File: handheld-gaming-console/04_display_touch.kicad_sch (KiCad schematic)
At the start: 3 parts, among them J7 DSI_15PIN_FPC

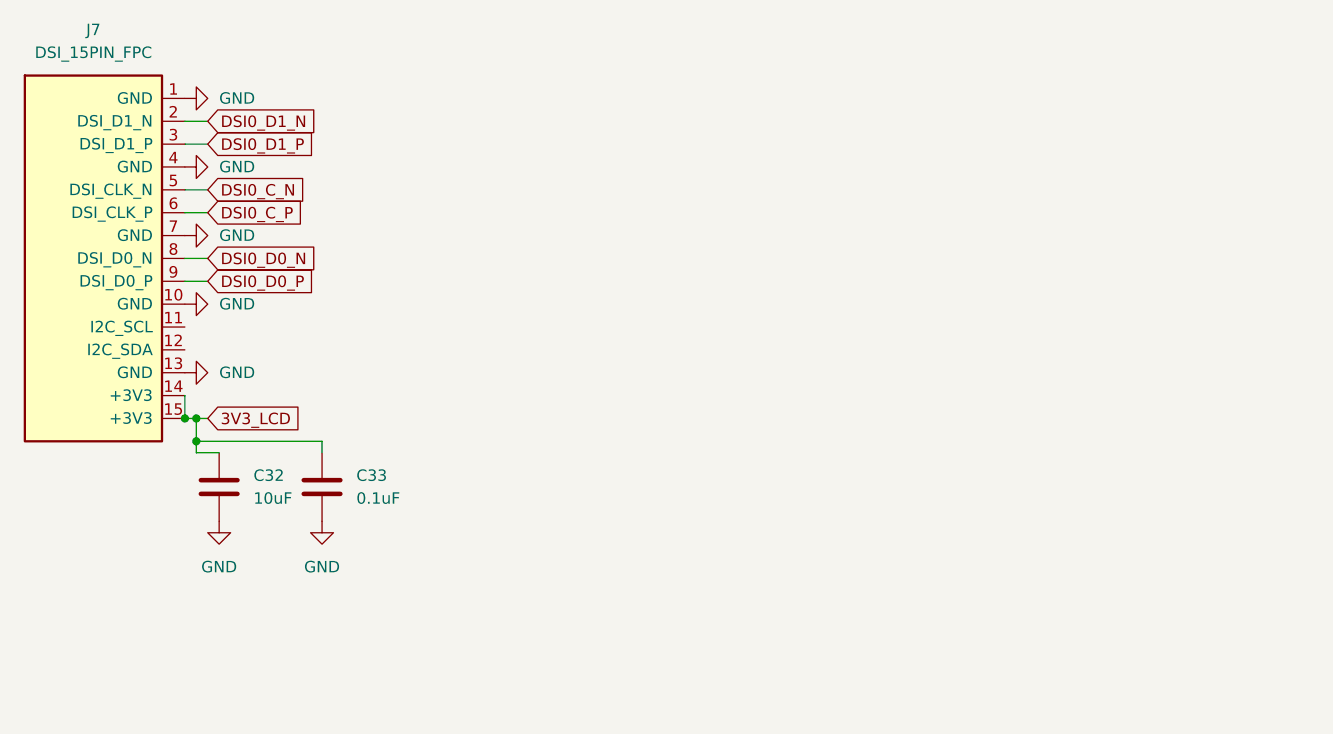
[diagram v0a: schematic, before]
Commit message: feat(display): implement 3V3_LCD power switch and GT911 I2C pull-ups with address strap
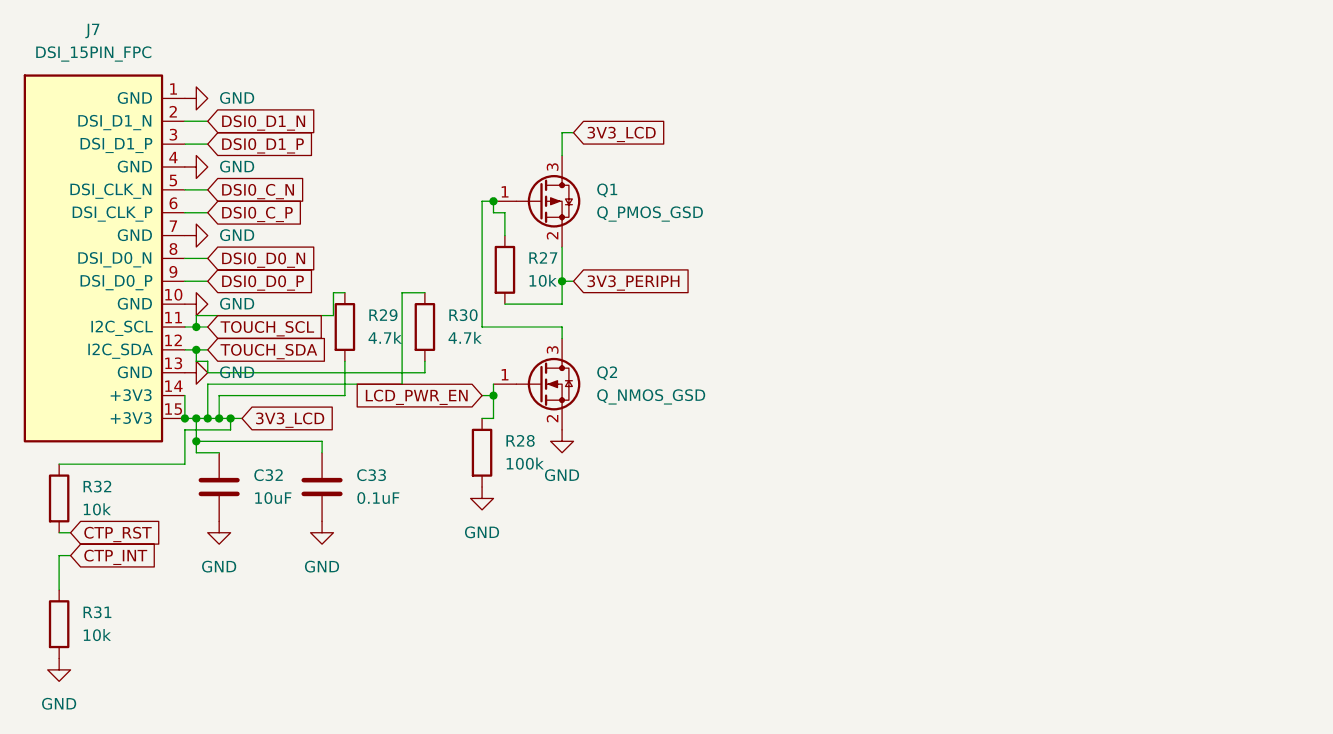
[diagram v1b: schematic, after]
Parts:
- added Q1: Q_PMOS_GSD, symbol Transistor_FET:Q_PMOS_GSD
- added Q2: Q_NMOS_GSD, symbol Transistor_FET:Q_NMOS_GSD
- added R27, R31, R32: 10k, symbol Device:R
- added R28: 100k, symbol Device:R
- added R29, R30: 4.7k, symbol Device:R
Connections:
- net 3V3_LCD: now also Q1.3 (D), R29.2, R30.1, R32.1
- net GND: now also Q2.2 (S), R28.2, R31.2
- net TOUCH_SCL: now reaches J7.11 (I2C_SCL)
- net TOUCH_SCL: now also R29.1
- net TOUCH_SDA: now reaches J7.12 (I2C_SDA)
- net TOUCH_SDA: now also R30.2
- new net: Q1.1 (G), Q2.3 (D), R27.1
- new net 3V3_PERIPH: Q1.2 (S), R27.2
- new net CTP_INT: R31.1
- new net CTP_RST: R32.2
- new net LCD_PWR_EN: Q2.1 (G), R28.1

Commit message: feat(display): implement AP3031 38V constant-current WLED backlight boost driver with PWM dimming and aux header
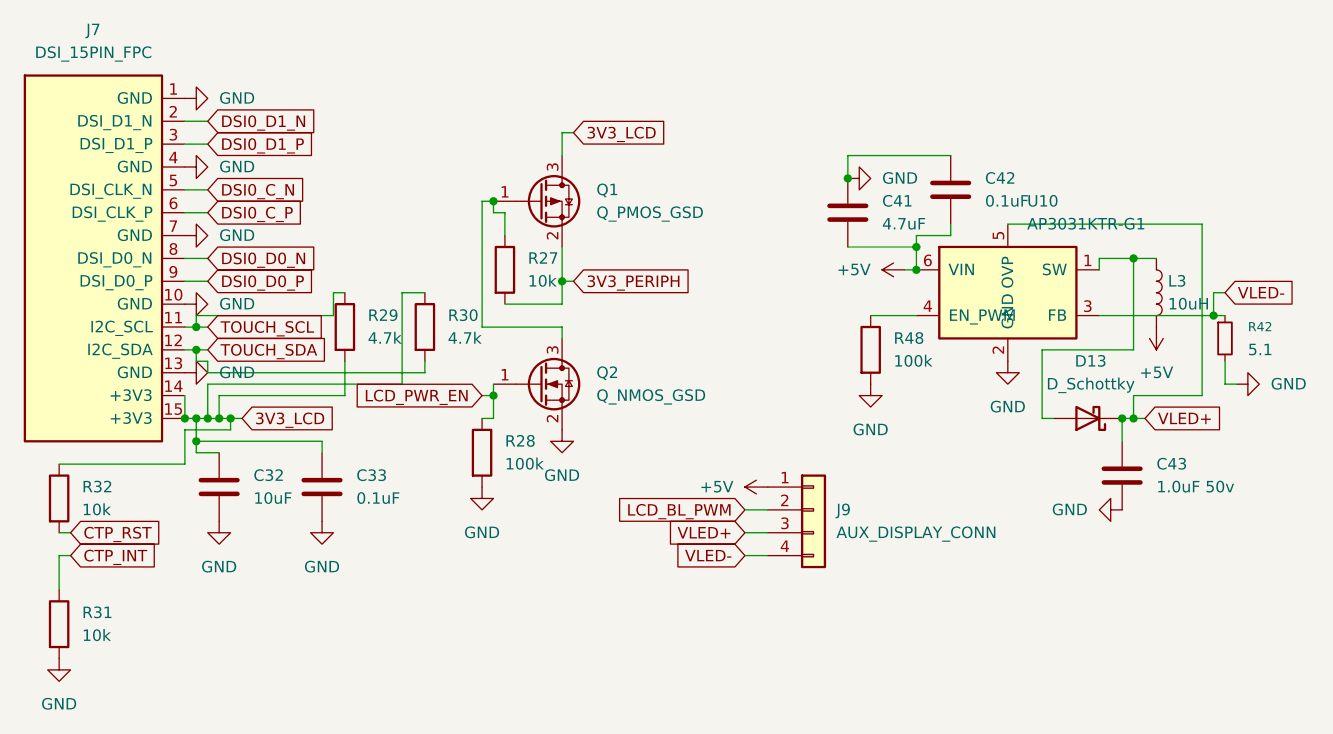
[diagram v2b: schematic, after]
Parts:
- added C41: 4.7uF, symbol Device:C
- added C42: 0.1uF, symbol Device:C
- added C43: 1.0uF 50v, symbol Device:C
- added D13: D_Schottky, symbol Device:D_Schottky
- added J9: AUX_DISPLAY_CONN, symbol Connector_Generic:Conn_01x04
- added L3: 10uH, symbol Device:L
- added R42: 5.1, symbol Device:R_Small
- added R48: 100k, symbol Device:R
- added U10: AP3031KTR-G1, Package_TO_SOT_SMD:SOT-23-6, symbol custom-components:AP3031KTR-G1
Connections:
- net GND: now also C41.1, C42.1, C43.2, R42.2, R48.2, U10.2 (GND)
- new net: D13.2 (A), L3.1, U10.1 (SW)
- new net: R48.1, U10.4 (EN_PWM)
- new net +5V: C41.2, C42.2, J9.1 (Pin_1), L3.2, U10.6 (VIN)
- new net LCD_BL_PWM: J9.2 (Pin_2)
- new net VLED+: C43.1, D13.1 (K), J9.3 (Pin_3), U10.5 (OVP)
- new net VLED-: J9.4 (Pin_4), R42.1, U10.3 (FB)
